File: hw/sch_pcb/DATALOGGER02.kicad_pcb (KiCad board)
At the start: 2 copper layers, 80.8 x 101.1 mm, 90 parts, among them J1 HEADER_2x01_PARALLEL, J10 HEADER_2x03_PARALLEL, J11 HEADER_2x01, J12 HEADER_2x01_PARALLEL, J13 HEADER_2x01_PARALLEL, J14 HEADER_2x01_PARALLEL, J15 HEADER_2x01_PARALLEL, J16 HEADER_2x01_PARALLEL, J17 HEADER_2x01_PARALLEL, J18 HEADER_2x01_PARALLEL, J19 HEADER_2x01_PARALLEL, J2 HEADER_2x01_PARALLEL, J20 HEADER_2x01_PARALLEL, J21 HEADER_2x01, J22 HEADER_2x01_PARALLEL, J23 HEADER_2x01_PARALLEL, J24 HEADER_2x01_PARALLEL, J25 HEADER_2x01_PARALLEL, J26 HEADER_2x01_PARALLEL, J27 HEADER_2x01_PARALLEL, J28 HEADER_2x01_PARALLEL, J29 HEADER_2x01_PARALLEL, J3 HEADER_2x01_PARALLEL, J30 HEADER_2x01_PARALLEL, J31 HEADER_2x03, J32 HEADER_2x01, J33 HEADER_2x03_PARALLEL, J34 MCC-SD (kouka z modulu), J4 HEADER_2x01_PARALLEL, J5 HEADER_2x01_PARALLEL, J6 HEADER_2x03_PARALLEL, J7 MCC-SD, J8 HEADER_2x01_PARALLEL, J9 HEADER_2x01, M2 HOLE, M3 HOLE, M4 HOLE, SW1 5MS1S102AM6QE, U1 ISL21080CIH320Z-TK, U2 TPS22965-Q1, U3 ATMEGA1284P-AU, U4 PCF85263A, U5 LM4041CIM3-1.2(neosazovat), U6 AT24CS64-SSHM, Y1 16MHz, Y2 ABS07-120-32.768KHZ-T

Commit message: progress?
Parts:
- removed BT2: BX0037, Mlab_Batery:BX0037
- removed BT3: Battery_Cell-device, Mlab_Batery:CH28-2032
- removed C11: 10uF, Mlab_R:SMD-0805
- removed C12: 1nF, Mlab_R:SMD-0805
- removed C13: 100nF, Mlab_R:SMD-0805
- removed D3: HLMP-K150+FIX-LED-313, Mlab_D:FIX-LED-313
- removed F2: 750mA, Mlab_F:1812
- removed J14, J15, J16, J17, J18, J22, J25, J26, J27, J28, J29, J30: HEADER_2x01_PARALLEL, Mlab_Pin_Headers:Straight_2x01
- removed J21, J32: HEADER_2x01, Mlab_Pin_Headers:Straight_2x01
- removed J31: HEADER_2x03, Mlab_Pin_Headers:Straight_2x03
- removed J33: HEADER_2x03_PARALLEL, Mlab_Pin_Headers:Straight_2x03
- removed J34: MCC-SD (kouka z modulu), Mlab_CON:MCC-SD
- removed M2, M3, M4: HOLE, Mlab_Mechanical:MountingHole_3mm
- removed R12: 0R, Mlab_R:SMD-0805
- removed R4: 100, Mlab_R:SMD-0805
- removed R7: 10k, Mlab_R:SMD-0805
- removed SW1: 5MS1S102AM6QE, Mlab_SW:5MS1S102AM6QE
- removed Y1: 16MHz, Mlab_XTAL:Crystal_HC49-U_Vertical
- added C23: 10uF, Mlab_C:SMD-0805, B.Cu at (74.7, 113.5)
- added C24: 100nF, Mlab_C:SMD-0805, B.Cu at (124.5, 116.6)
- added C25: 100nF, Mlab_C:SMD-0805, B.Cu at (76.7, 113.5)
- added C26: 1nF, Mlab_C:SMD-0805, B.Cu at (119.4, 101.9)
- added C27: 1uF, Mlab_C:SMD-0805, B.Cu at (81.9, 111.3)
- added C28: 50F, Mlab_C:C_Radial_D16_L25_P7.5, F.Cu at (130.3, 86.9)
- added C29: 100uF, Mlab_C:TantalC_SizeC_Reflow, B.Cu at (136.2, 97.3)
- added C30: EMI_Filter_C, Mlab_L:FIR_0805, B.Cu at (136.1, 93.5)
- added C31: 1uF, Mlab_C:SMD-0805, B.Cu at (88.2, 113.1)
- added C32: 100nF, Mlab_C:SMD-0805, B.Cu at (140.0, 92.4)
- added C33: 47uF, Mlab_C:TantalC_SizeB_Reflow, B.Cu at (134.9, 124.5)
- added C34: 47uF, Mlab_C:TantalC_SizeB_Reflow, B.Cu at (129.3, 117.7)
- added C35: EMI_Filter_C, Mlab_L:FIR_0805, B.Cu at (140.0, 125.4)
- added C36: EMI_Filter_C, Mlab_L:FIR_0805, B.Cu at (135.7, 116.1)
- added C37: 100nF, Mlab_C:SMD-0805, B.Cu at (140.0, 121.5)
- added C38: 100nF, Mlab_C:SMD-0805, B.Cu at (140.0, 118.2)
- added C39: 22uF, Mlab_C:TantalC_SizeB_Reflow, B.Cu at (129.8, 123.8)
- added C40: 22uF, Mlab_C:TantalC_SizeB_Reflow, B.Cu at (132.1, 130.9)
- added C41: -, Mlab_C:SMD-0805, B.Cu at (80.3, 84.6)
- added C42: -, Mlab_C:SMD-0805, B.Cu at (84.8, 87.1)
- added C43: 470nF, Mlab_C:SMD-0805, B.Cu at (88.5, 90.7)
- added C44: 1uF, Mlab_C:SMD-0805, B.Cu at (86.6, 94.0)
- added C45: 100nF, Mlab_C:SMD-0805, B.Cu at (79.0, 87.4)
- added C46: 47nF, Mlab_C:SMD-0805, B.Cu at (74.9, 86.9)
- added C47: 1p8, Mlab_C:SMD-0805, B.Cu at (72.1, 96.7)
- added C48: 47pF, Mlab_C:SMD-0805, B.Cu at (77.0, 86.8)
- added C49: 2p4, Mlab_C:SMD-0805, B.Cu at (73.2, 94.0)
- added C50: -, Mlab_C:SMD-0805, B.Cu at (77.2, 93.7)
- added C51: -, Mlab_C:SMD-0805, B.Cu at (71.1, 94.0)
- added C52: 3p3, Mlab_C:SMD-0805, B.Cu at (75.0, 89.7)
- added C53: 5p6, Mlab_C:SMD-0805, B.Cu at (75.2, 93.7)
- added C54: 39pF, Mlab_C:SMD-0805, B.Cu at (71.6, 89.7)
- added C55: 2p2, Mlab_C:SMD-0805, B.Cu at (68.1, 89.4)
- added C56: 1nF, Mlab_C:SMD-0805, B.Cu at (68.1, 94.7)
- added C57: 39pF, Mlab_C:SMD-0805, B.Cu at (64.5, 92.1)
- added C58: 3p3, Mlab_C:SMD-0805, B.Cu at (65.3, 95.0)
- added C59: 3p3, Mlab_C:SMD-0805, B.Cu at (61.5, 94.3)
- added D1: HLMP-K150+FIX-LED-313, Mlab_D:LED_1206_mill, B.Cu at (148.3, 90.2)
- added FID1: Fiducial, Fiducial:Fiducial_1mm_Mask2mm, F.Cu at (98.9, 103.7)
- added FID2: Fiducial, Fiducial:Fiducial_1mm_Mask2mm, F.Cu at (116.6, 112.0)
- added H1: MountingHole_Pad, Mlab_Mechanical:MountingHole_3mm, F.Cu at (55.9, 132.1)
- added H2: MountingHole_Pad, Mlab_Mechanical:MountingHole_3mm, F.Cu at (147.3, 132.1)
- added H3: MountingHole_Pad, Mlab_Mechanical:MountingHole_3mm, F.Cu at (147.3, 81.3)
- added H4: MountingHole_Pad, Mlab_Mechanical:MountingHole_3mm, F.Cu at (55.9, 81.3)
- added IC1: CY15B108QN-40SXI, Mlab_IO:SOIC-8_3.9x4.9mm_Pitch1.27mm, B.Cu at (118.0, 91.6)
- added IC2: FM3164-G, Mlab_IO:SOIC-14, B.Cu at (119.6, 121.7)
- added IC3: LTC4041EUFD#PBF, Package_DFN_QFN:QFN-24-1EP_4x5mm_P0.5mm_EP2.65x3.65mm, B.Cu at (126.5, 103.4)
- added JP1: SolderJumper_3_Bridged12, Jumper:SolderJumper-3_P1.3mm_Bridged12_RoundedPad1.0x1.5mm_NumberLabels, F.Cu at (123.0, 122.7)
- added JP2: SolderJumper_3_Bridged12, Jumper:SolderJumper-3_P1.3mm_Bridged12_RoundedPad1.0x1.5mm_NumberLabels, F.Cu at (117.6, 122.7)
- added JP3: SolderJumper_3_Bridged12, Jumper:SolderJumper-3_P1.3mm_Bridged12_RoundedPad1.0x1.5mm_NumberLabels, F.Cu at (86.1, 125.0)
- added JP4: SolderJumper_3_Bridged12, Jumper:SolderJumper-3_P1.3mm_Bridged12_RoundedPad1.0x1.5mm_NumberLabels, F.Cu at (108.4, 118.1)
- added L10: 4n7, Inductor_SMD:L_0402_1005Metric, B.Cu at (71.1, 91.4)
- added L11: 9n1, Inductor_SMD:L_0402_1005Metric, B.Cu at (61.5, 91.8)
- added L2: XAL-6030-182 1.8 uH, XAL6030181MEC:XAL6030181MEC, B.Cu at (126.5, 95.8)
- added L3: 1uH - DFE252012P-1R0M=P2, Inductor_SMD:L_1008_2520Metric, B.Cu at (140.0, 130.0)
- added L4: 1uH - DFE252012P-1R0M=P2, Inductor_SMD:L_1008_2520Metric, B.Cu at (136.1, 120.4)
- added L5: 15uH, Inductor_SMD:L_0402_1005Metric, B.Cu at (86.1, 91.2)
- added L6: 15nH, Inductor_SMD:L_0402_1005Metric, B.Cu at (74.4, 96.7)
- added L7: 0R, Inductor_SMD:L_0402_1005Metric, B.Cu at (77.7, 91.2)
- added L8: 47nH, Inductor_SMD:L_0402_1005Metric, B.Cu at (77.7, 89.9)
- added L9: 2n5, Inductor_SMD:L_0402_1005Metric, B.Cu at (75.5, 91.2)
- added Q1: DMP2045UQ-7, Package_TO_SOT_SMD:SOT-23, B.Cu at (71.5, 112.5)
- added Q2: SIR424DP, SIR424DP:SIR106DPT1RE3, B.Cu at (136.6, 110.0)
- added Q3: SIR424DP, SIR424DP:SIR106DPT1RE3, B.Cu at (136.6, 102.8)
- added R14: 10k, Mlab_R:SMD-0805, B.Cu at (98.6, 118.9)
- added R17: 10k, Mlab_R:SMD-0805, B.Cu at (104.6, 121.5)
- added R18: 10k, Mlab_R:SMD-0805, B.Cu at (89.7, 126.8)
- added R19: 10k, Mlab_R:SMD-0805, B.Cu at (91.7, 126.8)
- added R20: 470R, Mlab_R:SMD-0805, B.Cu at (68.3, 112.5)
- added R21: 10k, Mlab_R:SMD-0805, B.Cu at (116.1, 127.0)
- added R22: 150k, Mlab_R:SMD-0805, B.Cu at (113.0, 113.2)
- added R23: 56k, Mlab_R:SMD-0805, B.Cu at (113.1, 111.2)
- added R24: 100, Mlab_R:SMD-0805, B.Cu at (75.9, 119.9)
- added R25: 100, Mlab_R:SMD-0805, B.Cu at (76.0, 117.3)
- added R26: 100, Mlab_R:SMD-0805, B.Cu at (76.0, 110.0)
- added R27: 100, Mlab_R:SMD-0805, B.Cu at (73.2, 104.9)
- added R28: 2k2, Mlab_R:SMD-0805, B.Cu at (144.3, 89.3)
- added R29: 150k, Mlab_R:SMD-0805, B.Cu at (120.8, 97.8)
- added R30: 56k, Mlab_R:SMD-0805, B.Cu at (120.8, 95.8)
- added R31: 1M, Mlab_R:SMD-0805, B.Cu at (127.1, 113.5)
- added R32: 100k, Mlab_R:SMD-0805, B.Cu at (125.0, 108.5)
- added R33: 100k, Mlab_R:SMD-0805, B.Cu at (122.2, 108.8)
- added R34: 100k, Mlab_R:SMD-0805, B.Cu at (120.1, 108.8)
- added R35: 6.2k 1/8W, Mlab_R:SMD-0805, B.Cu at (121.7, 104.5)
- added R36: 2k, Mlab_R:SMD-0805, B.Cu at (130.3, 101.9)
- added R37: 25mR, Mlab_R:SMD-0805, B.Cu at (131.1, 105.2)
- added R38: 523k (E96), Mlab_R:SMD-0805, B.Cu at (128.3, 108.8)
- added R39: 100k, Mlab_R:SMD-0805, B.Cu at (119.4, 99.8)
- added R40: 220k, Mlab_R:SMD-0805, B.Cu at (126.2, 111.5)
- added R41: 100k, Mlab_R:SMD-0805, B.Cu at (123.4, 112.6)
- added R42: 806k, Mlab_R:SMD-0805, B.Cu at (136.9, 127.5)
- added R43: 91k, Mlab_R:SMD-0805, B.Cu at (133.2, 127.6)
- added R44: 511k, Mlab_R:SMD-0805, B.Cu at (133.2, 118.2)
- added R45: 91k, Mlab_R:SMD-0805, B.Cu at (132.3, 115.5)
- added R46: 10k, Mlab_R:SMD-0805, B.Cu at (83.6, 96.8)
- added R47: 100R, Mlab_R:SMD-0805, B.Cu at (68.1, 96.7)
- added R48: 10k, Mlab_R:SMD-0805, B.Cu at (92.4, 95.8)
- added U10: TPS631000DRLR, Package_TO_SOT_SMD:SOT-583-8, B.Cu at (133.4, 120.5)
- added U11: SX1262, Package_DFN_QFN:QFN-24-1EP_4x4mm_P0.5mm_EP2.6x2.6mm_ThermalVias, B.Cu at (82.0, 92.0)
- added U12: PE4259, Package_TO_SOT_SMD:SOT-363_SC-70-6, B.Cu at (68.3, 92.0)
- added U7: MS5611-01BA, Package_LGA:LGA-8_3x5mm_P1.25mm, B.Cu at (86.0, 120.8)
- added U8: MIC5504-1.8YM5-TR, Package_TO_SOT_SMD:SOT-23-5, B.Cu at (85.0, 111.0)
- added U9: TPS631000DRLR, Package_TO_SOT_SMD:SOT-583-8, B.Cu at (136.9, 130.0)
- added Y3: 32MHz, Mlab_XTAL:Crystal_SMD_NX2016SA, B.Cu at (82.0, 87.1)
- added Y6: 8MHz LFXTAL083138, Mlab_XTAL:Crystal SMD CFPX-180, B.Cu at (109.4, 104.9)
- BT1: value BX0037 -> Battery_Cell-device 3V; footprint Mlab_Batery:BX0037 -> Battery:BatteryHolder_Keystone_2998_1x6.8mm; moved to B.Cu
- C1, C15, C17, C18, C19, C2, C22, C5, C6: footprint Mlab_R:SMD-0805 -> Mlab_C:SMD-0805
- C10: value EMI_Filter_C -> 100nF; footprint Mlab_L:FIR1 -> Mlab_C:SMD-0805
- C14: value 10uF -> 100nF; footprint Mlab_R:SMD-0805 -> Mlab_C:SMD-0805
- C16: value 4u7 -> 100nF; footprint Mlab_R:SMD-0805 -> Mlab_C:SMD-0805
- C20: value 100nF -> 1uF; footprint Mlab_R:SMD-0805 -> Mlab_C:SMD-0805
- C21: value 100nF -> 1nF; footprint Mlab_R:SMD-0805 -> Mlab_C:SMD-0805
- C3, C4: value 100nF -> 15pF; footprint Mlab_R:SMD-0805 -> Mlab_C:SMD-0805
- C7: value 1uF -> 10uF; footprint Mlab_R:SMD-0805 -> Mlab_C:SMD-0805
- C8: value 100nF -> 4u7; footprint Mlab_R:SMD-0805 -> Mlab_C:SMD-0805
- C9: value 47uF -> 100nF; footprint Mlab_C:TantalC_SizeC_Reflow -> Mlab_C:SMD-0805
- D2: footprint Mlab_D:SMA_Standard -> Mlab_D:Diode-SMA_Standard
- F1: value 750mA -> 1.2A
- J10: value HEADER_2x03_PARALLEL -> HEADER_2x05_PARALLEL; footprint Mlab_Pin_Headers:Straight_2x03 -> Mlab_Pin_Headers:Straight_2x05
- J11: value HEADER_2x01 -> HEADER_2x07_PARALLEL; footprint Mlab_Pin_Headers:Straight_2x01 -> Mlab_Pin_Headers:Straight_2x07
- J12: value HEADER_2x01_PARALLEL -> HEADER_2x05_PARALLEL; footprint Mlab_Pin_Headers:Straight_2x01 -> Mlab_Pin_Headers:Straight_2x05
- J13: value HEADER_2x01_PARALLEL -> HEADER_2x02_PARALLEL; footprint Mlab_Pin_Headers:Straight_2x01 -> Mlab_Pin_Headers:Straight_2x02
- J19, J20: value HEADER_2x01_PARALLEL -> Conn_01x03_Male; footprint Mlab_Pin_Headers:Straight_2x01 -> Mlab_Pin_Headers:Straight_1x03
- J2: value HEADER_2x01_PARALLEL -> HEADER_2x01
- J23: value HEADER_2x01_PARALLEL -> MCX; footprint Mlab_Pin_Headers:Straight_2x01 -> Mlab_CON:MCX
- J24, J4, J5: value HEADER_2x01_PARALLEL -> HEADER_2x03_PARALLEL; footprint Mlab_Pin_Headers:Straight_2x01 -> Mlab_Pin_Headers:Straight_2x03
- J3: value HEADER_2x01_PARALLEL -> HEADER_2x03; footprint Mlab_Pin_Headers:Straight_2x01 -> Mlab_Pin_Headers:Straight_2x03
- J6: value HEADER_2x03_PARALLEL -> MCC-SD (kouka z modulu); footprint Mlab_Pin_Headers:Straight_2x03 -> Mlab_CON:MCC-SD
- J7: value MCC-SD -> Conn_01x06_Female; footprint Connector_Card:SD_TE_2041021 -> Connector_JST:JST_GH_SM06B-GHS-TB_1x06-1MP_P1.25mm_Horizontal; moved to F.Cu
- J8: value HEADER_2x01_PARALLEL -> Conn_01x07_Female; footprint Mlab_Pin_Headers:Straight_2x01 -> Connector_JST:JST_GH_SM07B-GHS-TB_1x07-1MP_P1.25mm_Horizontal
- J9: value HEADER_2x01 -> Conn_01x04_Female; footprint Mlab_Pin_Headers:Straight_2x01 -> Connector_JST:JST_GH_SM04B-GHS-TB_1x04-1MP_P1.25mm_Horizontal
- R1: value 100 -> -
- R10: value 2k2 -> 10k
- R11, R16, R8: value - -> 10k
- R15: value 0R -> 10k
- R2: value 100 -> 4k7
- R3: value 100 -> 10k
- R5: value 4k7 -> 10k
- U2: value TPS22965-Q1 -> LM4041CIM3-1.2(neosazovat); footprint Package_SON:WSON-8-1EP_2x2mm_P0.5mm_EP0.9x1.6mm_ThermalVias -> Package_TO_SOT_SMD:SOT-23
- U4: value PCF85263A -> TXS0108EPW; footprint Mlab_IO:TSSOP-10_3x3mm_Pitch0.5mm -> Package_SO:TSSOP-20_4.4x6.5mm_P0.65mm
- U5: value LM4041CIM3-1.2(neosazovat) -> ICM-20948; footprint Package_TO_SOT_SMD:SOT-23 -> Sensor_Motion:InvenSense_QFN-24_3x3mm_P0.4mm
- U6: value AT24CS64-SSHM -> TPS22965-Q1; footprint Package_SO:SOIC-8_3.9x4.9mm_P1.27mm -> Package_SON:WSON-8-1EP_2x2mm_P0.5mm_EP0.9x1.6mm_ThermalVias
- Y2: value ABS07-120-32.768KHZ-T -> 6pF crystal - 32.768kHz
- moved J6 118.5 mm to (64.8, 113.0), turned to -90 degrees
- moved C5 108.7 mm to (78.5, 99.6), turned to 90 degrees
- moved C16 103.8 mm to (91.4, 122.2)
- moved J23 102.9 mm to (55.9, 91.9), turned to 0 degrees
- moved J2 99.4 mm to (82.1, 102.8), turned to 0 degrees
- moved U2 91.1 mm to (81.7, 99.6)
- moved J9 88.4 mm to (107.1, 133.1), turned to 0 degrees
- moved J4 88.0 mm to (96.0, 80.3), turned to 90 degrees
- moved J10 87.7 mm to (95.2, 133.1), turned to -90 degrees
- moved J12 87.5 mm to (81.8, 133.1)
- moved C22 85.5 mm to (88.9, 120.2), turned to -90 degrees
- moved R11 81.3 mm to (94.7, 111.5), turned to 0 degrees
- moved C19 80.6 mm to (109.0, 117.4), turned to 90 degrees
- moved C7 80.4 mm to (87.9, 103.9), turned to -90 degrees
- moved C21 80.3 mm to (94.6, 85.3), turned to 180 degrees
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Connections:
- net Net-(D2-Pad1) renamed UNREG_POWER_INPUT
- C1 pad 1: VDD -> +3.3V
- C10 pad 1: Net-(C10-Pad1) -> /Microcontroller/AVCC
- C14 pad 1: Net-(C14-Pad1) -> GND
- C14 pad 2: GND -> +1V8
- C15 pad 1: /SD_VDD -> +1V8
- C16 pad 1: /RST#_P -> +3.3V
- C16 pad 2: /RST# -> GND
- C17 pad 1: Net-(C14-Pad1) -> +3.3V
- C18 pad 1: VDD -> +3.3V
- C19 pad 1: VDD -> Net-(U5-REGOUT)
- C2 pad 1: VDD -> +3.3V
- C20 pad 1: VDD -> +3.3V
- C21 pad 1: VDD -> Net-(U6-CT)
- C22 pad 1: VDD -> +3.3V
- C3 pad 1: VDD -> GND
- C3 pad 2: GND -> Net-(U3-XTAL2)
- C4 pad 1: /AREF -> GND
- C4 pad 2: GND -> Net-(U3-XTAL1)
- C5 pad 1: Net-(C5-Pad1) -> /Microcontroller/AREF
- C6 pad 1: /AVCC -> +3.3V
- C7 pad 1: VDD -> Net-(U3-AREF)
- C8 pad 1: Net-(C8-Pad1) -> /Microcontroller/RST#_P
- C8 pad 2: GND -> /Microcontroller/RST#
- C9 pad 1: Net-(C10-Pad1) -> Net-(U3-AREF)
- J1 pad 1: GND -> /Microcontroller/RST#
- J1 pad 2: GND -> /Microcontroller/RST#
- J10 pad 3: Net-(J10-Pad3) -> SCL_I2C
- J10 pad 4: Net-(J10-Pad3) -> SCL_I2C
- J10 pad 5: GND -> +3.3V
- J10 pad 6: GND -> +3.3V
- J11 pad 1: Net-(J11-Pad1) -> GND
- J11 pad 2: /SD_VDD -> GND
- J12 pad 1: /PC2 -> GND
- J12 pad 2: /PC2 -> GND
- J13 pad 1: /PC3 -> /Telemetry/DIO3
- J13 pad 2: /PC3 -> /Telemetry/DIO3
- J19 pad 1: /RX1 -> GND
- J19 pad 2: /RX1 -> Net-(J19-Pin_2)
- J2 pad 1: /PC0 -> /Microcontroller/AREF
- J2 pad 2: /PC0 -> Net-(U3-AREF)
- J20 pad 1: /TX1 -> GND
- J20 pad 2: /TX1 -> Net-(J20-Pin_2)
- J23 pad 1: /PA1 -> Net-(C59-Pad2)
- J23 pad 2: /PA1 -> GND
- J24 pad 1: VDD -> GND
- J24 pad 2: VDD -> GND
- J3 pad 1: VDD -> MISO_SPI
- J3 pad 2: VDD -> +3.3V
- J4 pad 1: /PC1 -> GND
- J4 pad 2: /PC1 -> GND
- J6 pad 1: GND -> Net-(J6-CD/DAT3)
- J6 pad 2: GND -> Net-(J6-CMD)
- J6 pad 3: Net-(F2-Pad1) -> GND
- J6 pad 4: Net-(F2-Pad1) -> /Peripherals/sd_card_power
- J6 pad 5: GND -> Net-(J6-CLK)
- J7 pad 1: Net-(J34-Pad1) -> +5V
- J7 pad 2: Net-(J34-Pad2) -> RX1
- J7 pad 3: GND -> TX1
- J7 pad 4: /SD_VDD -> unconnected-(J7-Pin_4-Pad4)
- J7 pad 5: Net-(J34-Pad5) -> unconnected-(J7-Pin_5-Pad5)
- J8 pad 1: /RST# -> +5V
- J8 pad 2: /RST# -> SCK_SPI
- J9 pad 1: /AREF -> +5V
- J9 pad 2: Net-(C14-Pad1) -> SCL_I2C
- L1 pad 1: VDD -> +3.3V
- L1 pad 2: /AVCC -> /Microcontroller/AVCC
- R1 pad 1: Net-(J34-Pad1) -> Net-(U3-XTAL1)
- R1 pad 2: /PB4 -> +3.3V
- R10 pad 1: Net-(D3-Pad2) -> +3.3V
- R10 pad 2: /LED -> SCL_I2C
- R11 pad 1: VDD -> +3.3V
- R11 pad 2: Net-(R11-Pad2) -> SDA_I2C
- R15 pad 1: GND -> +1V8
- R15 pad 2: Net-(R15-Pad2) -> /Peripherals/SCL_I2C_1V8
- R16 pad 1: Net-(R15-Pad2) -> +1V8
- R16 pad 2: VDD -> /Peripherals/AUX_SDA_1V8
- R2 pad 1: Net-(J34-Pad2) -> /Microcontroller/AREF
- R2 pad 2: /PB5 -> +3.3V
- R3 pad 1: Net-(J34-Pad5) -> /Microcontroller/RST#_P
- R3 pad 2: /PB7 -> +3.3V
- R5 pad 1: /AREF -> +3.3V
- R5 pad 2: VDD -> CS_CONN_1
- R6 pad 1: /PC1 -> +3.3V
- R6 pad 2: VDD -> CS_FRAM
- R8 pad 1: VDD -> +3.3V
- R8 pad 2: Net-(C8-Pad1) -> CS_CONN_2
- R9 pad 1: /RST#_P -> +3.3V
- R9 pad 2: VDD -> CS_SDCARD
- U1 pad 1: VDD -> +3.3V
- U1 pad 2: /AREF -> /Microcontroller/AREF
- U2 pad 1: VDD -> /Microcontroller/AREF
- U2 pad 2: VDD -> GND
- U2 pad 3: /PA2 -> (no net)
- U3 pad 1: /PB5 -> MOSI_SPI
- U3 pad 10: /TX0 -> TX0
- U3 pad 11: /RX1 -> RX1
- U3 pad 12: /TX1 -> TX1
- U3 pad 13: (no net) -> CNT2
- U3 pad 14: (no net) -> unconnected-(U3-(PCINT294/OC1A)PD5-Pad14)
- U3 pad 15: (no net) -> unconnected-(U3-(PCINT30/OC2B/ICP)PD6-Pad15)
- U3 pad 16: (no net) -> INT1
- U3 pad 17: VDD -> +3.3V
- U3 pad 19: /PC0 -> SCL_I2C
- U3 pad 2: /PB6 -> MISO_SPI
- U3 pad 20: /PC1 -> SDA_I2C
- U3 pad 21: /PC2 -> PFO
- U3 pad 22: /PC3 -> CAPGD
- U3 pad 23: /INT -> SYSGD
- U3 pad 24: /PC5 -> CAPFLT
- U3 pad 25: /PC6 -> unconnected-(U3-(PCINT22/TOSC1)PC6-Pad25)
- U3 pad 26: /LED -> LED
- U3 pad 27: /AVCC -> /Microcontroller/AVCC
- U3 pad 29: Net-(C14-Pad1) -> Net-(U3-AREF)
- U3 pad 3: /PB7 -> SCK_SPI
- U3 pad 30: (no net) -> RST_LORA
- U3 pad 31: (no net) -> DIO_LORA
- U3 pad 32: (no net) -> BUSY_LORA
- U3 pad 33: (no net) -> CS_LORA
- U3 pad 34: (no net) -> IO_SWCH
- U3 pad 35: /PA2 -> PA2
- U3 pad 36: /PA1 -> PA1
- U3 pad 37: /PA0 -> PA0
- U3 pad 38: VDD -> +3.3V
- U3 pad 4: /RST#_P -> /Microcontroller/RST#_P
- U3 pad 40: /PB0 -> WP_FRAM
- U3 pad 41: Net-(J11-Pad1) -> CS_CONN_1
- U3 pad 42: Net-(J11-Pad1) -> CS_FRAM
- U3 pad 43: Net-(J11-Pad1) -> CS_CONN_2
- U3 pad 44: /PB4 -> CS_SDCARD
- U3 pad 5: VDD -> +3.3V
- U3 pad 7: Net-(C5-Pad1) -> Net-(U3-XTAL2)
- U3 pad 8: Net-(C8-Pad1) -> Net-(U3-XTAL1)
- U3 pad 9: /RX0 -> RX0
- U4 pad 1: Net-(U4-Pad1) -> /Peripherals/SDA_I2C_1V8
- U4 pad 10: VDD -> +1V8
- U4 pad 2: Net-(U4-Pad2) -> +1V8
- U4 pad 3: Net-(BT3-Pad1) -> GND
- U4 pad 4: (no net) -> /Peripherals/SCL_I2C_1V8
- U4 pad 6: /PC1 -> /Peripherals/AUX_SDA_1V8
- U4 pad 7: /PC0 -> GND
- U4 pad 8: (no net) -> /Peripherals/AUX_SCL_1V8
- U4 pad 9: /INTA -> /Peripherals/INT1_1V8
- U5 pad 1: /AREF -> unconnected-(U5-NC-Pad1)
- U5 pad 2: GND -> unconnected-(U5-NC-Pad2)
- U5 pad 3: (no net) -> unconnected-(U5-NC-Pad3)
- U6 pad 1: Net-(R11-Pad2) -> +3.3V
- U6 pad 2: GND -> +3.3V
- U6 pad 3: GND -> IO_SWCH
- U6 pad 4: GND -> +3.3V
- U6 pad 5: /PC1 -> GND
- U6 pad 6: /PC0 -> Net-(U6-CT)
- U6 pad 7: Net-(R15-Pad2) -> Net-(J4-Pad3)
- U6 pad 8: VDD -> Net-(J4-Pad3)
- Y2 pad 1: Net-(U4-Pad2) -> Net-(IC2-X1)
- Y2 pad 2: Net-(U4-Pad1) -> Net-(IC2-X2)
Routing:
- net GND: track 435.8 -> 14.7 mm, vias 191 -> 39
- net +3.3V: track 0.00 -> 347.2 mm, vias 0 -> 23
- net VDD: track 245.9 -> 0.00 mm, vias 8 -> 0
- net +5V: track 0.00 -> 148.4 mm, vias 0 -> 4
- net MOSI_SPI: track 0.00 -> 105.4 mm, vias 0 -> 3
- net MISO_SPI: track 0.00 -> 102.7 mm, vias 0 -> 4
- net Net-(J11-Pad1): track 100.3 -> 0.00 mm, vias 1 -> 0
- net SCL_I2C: track 0.00 -> 97.5 mm, vias 0 -> 3
- net /Power_management/Vdc: track 0.00 -> 94.9 mm, vias 0 -> 1
- net SCK_SPI: track 0.00 -> 91.8 mm, vias 0 -> 3
- net /LED: track 85.8 -> 0.00 mm, vias 2 -> 0
- net SDA_I2C: track 0.00 -> 84.1 mm, vias 0 -> 1
- net /PB5: track 80.1 -> 0.00 mm, vias 3 -> 0
- net /PB6: track 79.4 -> 0.00 mm, vias 3 -> 0
- net /PB7: track 76.1 -> 0.00 mm, vias 2 -> 0
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- added copper zone on In1.Cu, net GND
- added copper zone on In2.Cu, net GND
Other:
- board size 80.8 x 101.1 mm -> 101.1 x 60.5 mm
- copper layers 2 -> 4
- board text removed: "2018"
- board text removed: "AREF"
- board text removed: "AREF_IN"
- board text removed: "ATMEL ISP"
- board text removed: "BATERY"
- board text removed: "DATALOGGER01A"
- board text removed: "GND"
- board text removed: "INT"
- board text removed: "INTA"
- board text removed: "JACHO"
- board text removed: "MLAB.CZ"
- board text removed: "ON"
- board text removed: "PA0"
- board text removed: "PA1"
- board text removed: "PB0"
- board text removed: "PB5"
- board text removed: "PB6"
- board text removed: "PB7"
- board text removed: "PC2"
- board text removed: "PC3"
- board text removed: "PC5"
- board text removed: "PC6"
- board text removed: "POWER IN"
- board text removed: "RST#"
- board text removed: "RX0"
- board text removed: "RX1"
- board text removed: "SCL"
- board text removed: "SDA"
- board text removed: "SDVDD"
- board text removed: "SW POWER"
- board text removed: "TX0"
- board text removed: "TX1"
- board text removed: "VDD"

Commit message: another updates
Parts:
- moved C8 0.21 mm to (111.4, 101.3)
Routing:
- net +3.3V: track 347.2 -> 377.0 mm, vias 23 -> 24
- net /Microcontroller/RST#_P: track 8.59 -> 37.8 mm, vias 0 -> 1
- net GND: track 14.7 -> 29.6 mm, vias 39 -> 122
- net /Microcontroller/RST#: track 0.00 -> 8.52 mm
- net +1V8: track 45.6 -> 52.3 mm, vias 5 -> 6
- net Net-(U3-XTAL2): track 6.15 -> 8.14 mm
- net CS_SDCARD: track 47.2 -> 48.9 mm
- net CNT2: track 32.7 -> 33.4 mm
- net (no net): vias 83 -> 11

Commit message: silkmasks done
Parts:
- U12: value PE4259 -> U12
- U8: value MIC5504-1.8YM5-TR -> r
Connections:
- J13 pad 1: /Telemetry/DIO3 -> /Telemetry/DIO1
- J13 pad 2: /Telemetry/DIO3 -> /Telemetry/DIO1
- J13 pad 3: /Telemetry/DIO1 -> /Telemetry/DIO3
- J13 pad 4: /Telemetry/DIO1 -> /Telemetry/DIO3
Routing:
- net DIO_LORA: track 0.00 -> 52.7 mm, vias 0 -> 4
- net Net-(IC3-SCAP): track 15.5 -> 39.7 mm, vias 0 -> 2
- net /Telemetry/DIO1: track 0.00 -> 24.2 mm, vias 0 -> 1
- net /Telemetry/DIO3: track 0.00 -> 19.5 mm, vias 0 -> 1
- net GND: track 29.6 -> 47.8 mm, vias 122 -> 139
- net +3.3V: track 377.0 -> 392.9 mm, vias 24 -> 25
- net +1V8: track 52.3 -> 64.0 mm, vias 6 -> 7
- net +5V: track 148.4 -> 153.5 mm
- net Net-(U11-VR_PA): track 2.22 -> 6.96 mm
- net Net-(IC3-VIN): track 14.1 -> 15.0 mm
- net CS_SDCARD: track 48.9 -> 48.0 mm
- net Net-(IC3-CLN): track 7.22 -> 7.73 mm
- net (no net): vias 11 -> 2
- added copper zone on In1.Cu, net +3.3V
- removed copper zone on In1.Cu, net GND
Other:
- board text added: "+5V"
- board text added: "3V3"
- board text added: "3V3 BUBO DIS/EN"
- board text added: "5V BUBO DIS/EN"
- board text added: "AREF"
- board text added: "AREF_IN"
- board text added: "DIO1"
- board text added: "DIO3"
- board text added: "GND"
- board text added: "ICSP"
- board text added: "MISO|3V3"
- board text added: "PA0"
- board text added: "PA1"
- board text added: "PA2"
- board text added: "POWER IN"
- board text added: "PX4-I2C"
- board text added: "PX4-SPI"
- board text added: "PX4-UART"
- board text added: "RST#"
- board text added: "RST|GND"
- board text added: "SCK|MOSI"
- board text added: "SCL"
- board text added: "SDA"
- board text added: "SUPER CAP"
- board text added: "SWT"
- board text added: "VDC"
- board text added: "aSCL"
- board text added: "aSDA"

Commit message: checks 'passed'
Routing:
- net Net-(IC3-VSYS_1): track 16.3 -> 25.8 mm, vias 0 -> 2
- net GND: track 47.8 -> 54.7 mm, vias 139 -> 140
- net Net-(J6-CLK): track 0.00 -> 3.19 mm, vias 0 -> 1
- net Net-(U11-XTA): track 5.14 -> 7.20 mm
- net +3.3V: track 392.9 -> 394.4 mm
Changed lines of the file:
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@@
 	)
 	(via
+		(at 135.128 129.032)
+		(size 0.8)
+		(drill 0.4)
+		(layers "F.Cu" "B.Cu")
+		(net 1)
+	)
+	(via
 		(at 53.34 100.838)
 		(size 0.8)
@@
 	)
 	(segment
+		(start 82.772 90.6925)
+		(end 83.072 90.9925)
+		(width 0.25)
+		(layer "B.Cu")
+		(net 1)
+	)
+	(segment
+		(start 81.272 90.105)
+		(end 81.272 90.6925)
+		(width 0.25)
+		(layer "B.Cu")
+		(net 1)
+	)
+	(segment
 		(start 109.474 119.634)
 		(end 109.020338 119.634)
@@
 	)
 	(segment
+		(start 129.198 103.417)
+		(end 129.667 103.886)
+		(width 0.25)
+		(layer "B.Cu")
+		(net 1)
+	)
+	(segment
 		(start 69.21 91.9965)
 		(end 68.5315 91.9965)
@@
 	)
 	(segment
+		(start 135.128 129.0834)
+		(end 135.128 129.032)
+		(width 0.25)
+		(layer "B.Cu")
+		(net 1)
+	)
+	(segment
 		(start 79.62226 92.7925)
 		(end 79.347 93.06776)
@@
 	)
 	(segment
+		(start 128.43 103.417)
+		(end 129.198 103.417)
+		(width 0.25)
+		(layer "B.Cu")
+		(net 1)
+	)
+	(segment
+		(start 95.25 87.7)
+		(end 95.5 87.95)
+		(width 0.25)
+		(layer "B.Cu")
+		(net 1)
+	)
+	(segment
+		(start 80.0845 92.7925)
+		(end 80.672 92.7925)
+		(width 0.25)
+		(layer "B.Cu")
+		(net 1)
+	)
+	(segment
+		(start 82.772 90.105)
+		(end 82.772 90.6925)
+		(width 0.25)
+		(layer "B.Cu")
+		(net 1)
+	)
+	(segment
 		(start 93.843 121.942)
 		(end 94.72 121.942)
@@
 	)
 	(segment
+		(start 136.188 129.794)
+		(end 135.8386 129.794)
+		(width 0.25)
+		(layer "B.Cu")
+		(net 1)
+	)
+	(segment
+		(start 80.672 92.7925)
+		(end 80.972 93.0925)
+		(width 0.25)
+		(layer "B.Cu")
+		(net 1)
+	)
+	(segment
 		(start 80.78324 89.154)
 		(end 80.683604 89.154)
@@
 	)
 	(segment
+		(start 135.8386 129.794)
+		(end 135.128 129.0834)
+		(width 0.25)
+		(layer "B.Cu")
+		(net 1)
+	)
+	(segment
 		(start 99.568 123.242)
 		(end 98.35 123.242)
@@
 	)
 	(segment
+		(start 81.272 90.6925)
+		(end 80.972 90.9925)
+		(width 0.25)
+		(layer "B.Cu")
+		(net 1)
+	)
+	(segment
 		(start 68.5315 91.9965)
 		(end 68.326 92.202)
@@
 	)
 	(segment
+		(start 95.25 87)
+		(end 95.25 87.7)
+		(width 0.25)
+		(layer "B.Cu")
+		(net 1)
+	)
+	(segment
 		(start 104.648 103.734)
 		(end 103.226 103.734)
@@
 	)
 	(segment
+		(start 95.25 88.9)
+		(end 93.726 88.9)
+		(width 0.25)
+		(layer "B.Cu")
+		(net 3)
+	)
+	(segment
 		(start 83.9595 92.2925)
 		(end 84.4185 92.2925)
@@
 		(net 16)
 	)
+	(via
+		(at 128.27 107.823)
+		(size 0.8)
+		(drill 0.4)
+		(layers "F.Cu" "B.Cu")
+		(net 17)
+	)
+	(via
+		(at 128.524 100.076)
+		(size 0.8)
+		(drill 0.4)
+		(layers "F.Cu" "B.Cu")
+		(net 17)
+	)
+	(segment
+		(start 128.27 100.33)
+		(end 128.524 100.076)
+		(width 0.25)
+		(layer "In1.Cu")
+		(net 17)
+	)
+	(segment
+		(start 128.27 107.823)
+		(end 128.27 100.33)
+		(width 0.25)
+		(layer "In1.Cu")
+		(net 17)
+	)
 	(segment
 		(start 134.714 94.648)
@@
 	)
 	(segment
+		(start 127.48 100.485)
+		(end 127.48 100.967)
+		(width 0.25)
+		(layer "B.Cu")
+		(net 17)
+	)
+	(segment
 		(start 132.334 101.6)
 		(end 131.572 101.6)
@@
 	)
 	(segment
+		(start 127.889 100.076)
+		(end 127.48 100.485)
+		(width 0.25)
+		(layer "B.Cu")
+		(net 17)
+	)
+	(segment
+		(start 128.524 100.076)
+		(end 127.889 100.076)
+		(width 0.25)
+		(layer "B.Cu")
+		(net 17)
+	)
+	(segment
 		(start 132.334 100.33)
 		(end 132.334 101.6)
@@
 	)
 	(segment
+		(start 81.2165 86.5505)
+		(end 81.28 86.614)
+		(width 0.25)
+		(layer "B.Cu")
+		(net 22)
+	)
+	(segment
 		(start 80.518 88.352)
 		(end 80.555 88.389)
@@
 	)
 	(segment
+		(start 81.2165 84.582)
+		(end 81.2165 86.5505)
+		(width 0.25)
+		(layer "B.Cu")
+		(net 22)
+	)
+	(segment
 		(start 81.28 86.614)
 		(end 80.605 86.614)
@@
 	)
 	(segment
-		(start 135.179362 130.048)
+		(start 135.179362 130.429)
+		(end 135.560362 130.429)
+		(width 0.25)
+		(layer "F.Cu")
+		(net 83)
+	)
+	(segment
+		(start 135.560362 130.429)
 		(end 138.176 133.044638)
 		(width 0.25)
@@
 	)
 	(via
-		(at 135.179362 130.048)
+		(at 135.179362 130.429)
 		(size 0.8)
 		(drill 0.4)
@@
 	)
 	(segment
-		(start 136.188 130.294)
-		(end 135.425362 130.294)
+		(start 135.179362 130.429)
+		(end 135.314362 130.294)
 		(width 0.25)
 		(layer "B.Cu")
@@
 	)
 	(segment
-		(start 135.425362 130.294)
-		(end 135.179362 130.048)
+		(start 135.314362 130.294)
+		(end 136.188 130.294)
 		(width 0.25)
 		(layer "B.Cu")
@@
 	)
 	(segment
+		(start 77.856371 109.905)
+		(end 78.2796 110.328229)
+		(width 0.25)
+		(layer "F.Cu")
+		(net 134)
+	)
+	(segment
+		(start 76.73 109.905)
+		(end 77.856371 109.905)
+		(width 0.25)
+		(layer "F.Cu")
+		(net 134)
+	)
+	(via
+		(at 78.2796 110.328229)
+		(size 0.8)
+		(drill 0.4)
+		(layers "F.Cu" "B.Cu")
+		(net 134)
+	)
+	(segment
+		(start 76.962 109.982)
+		(end 77.933371 109.982)
+		(width 0.25)
+		(layer "B.Cu")
+		(net 134)
+	)
+	(segment
+		(start 77.933371 109.982)
+		(end 78.2796 110.328229)
+		(width 0.25)
+		(layer "B.Cu")
+		(net 134)
+	)
+	(segment

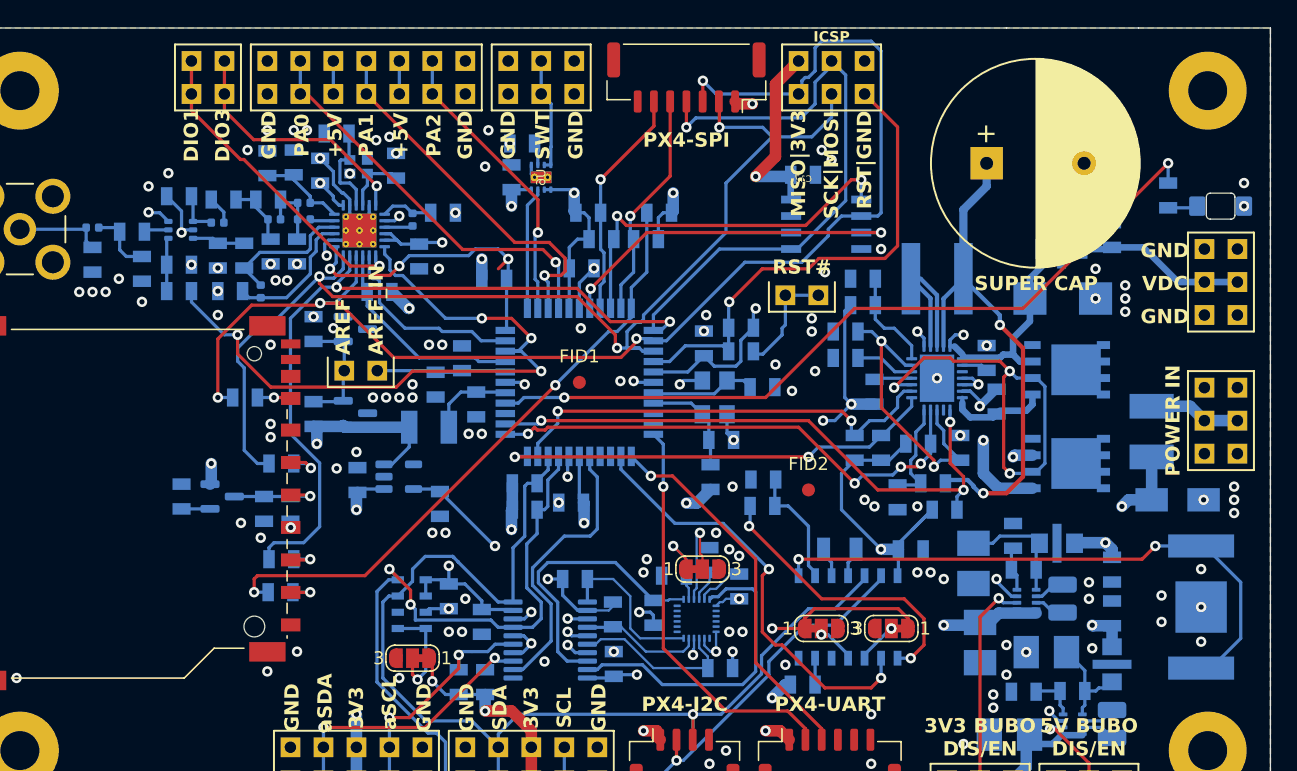
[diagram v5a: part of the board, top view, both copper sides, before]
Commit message: Update components from libraries. Improve schematics. Resolve some ERC and DRC errors.
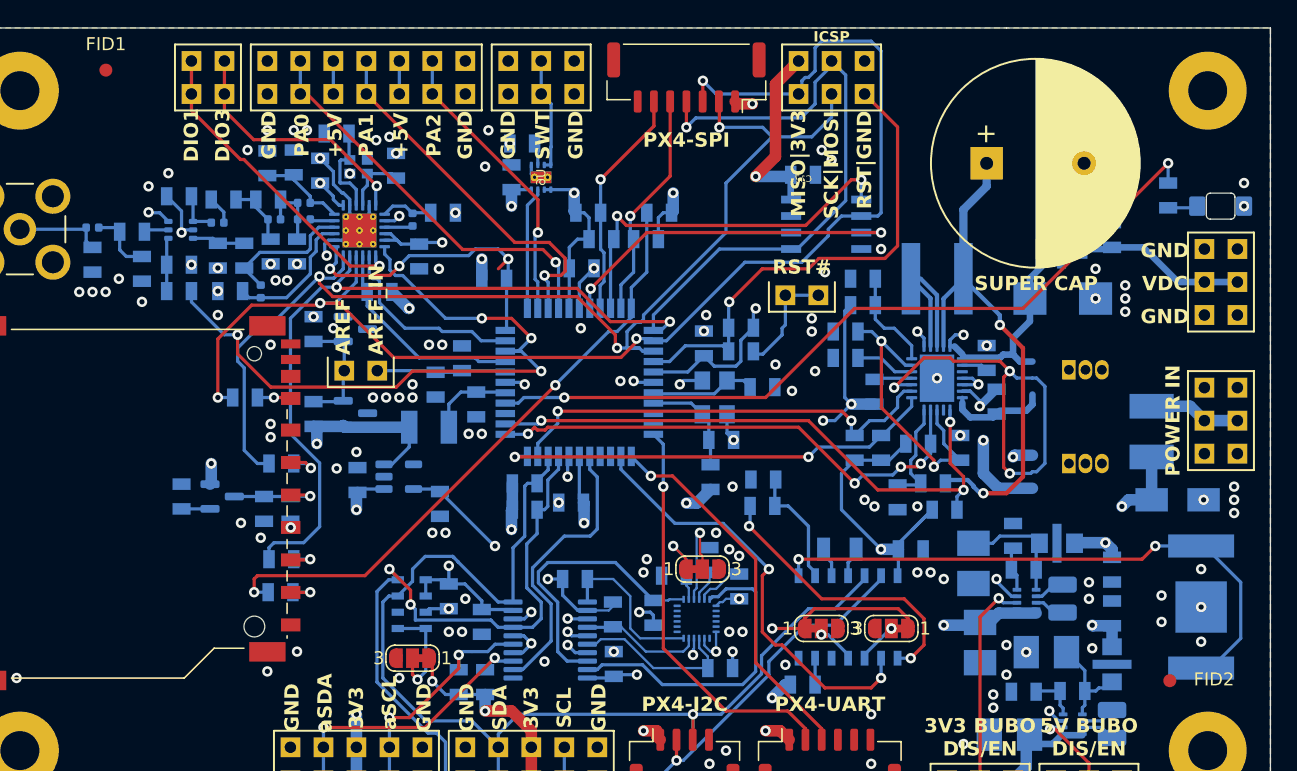
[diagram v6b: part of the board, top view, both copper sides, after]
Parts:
- Q2, Q3: footprint SIR424DP:SIR106DPT1RE3 -> Package_TO_SOT_THT:TO-92_Inline
- U12: value U12 -> PE4259
- U8: value r -> MIC5504-1.8YM5-TR
- moved FID1 43.7 mm to (62.5, 79.7)
- moved FID2 31.5 mm to (144.4, 126.7)
